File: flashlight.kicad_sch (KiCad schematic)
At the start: 42 parts, among them J1 USB_B_Micro, Q1 HSS2333, Q2 HSS2333, SW1 SW_DIP_x01, U1 LP4054HB5F, U2 MT3608

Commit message: v0.1
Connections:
- net GND: now also R3.1; no longer D3.1 (K)
- net at C1.1, D1.1 (K), D2.2 (A)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: now also U1.4 (V_{DD})
- net at R2.2, U1.1 (STAT): now also D3.2 (A); no longer R3.1
- net at R3.2: now also D3.1 (K); no longer D3.2 (A)
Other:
- moved on the sheet: D3, R3
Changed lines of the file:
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@@
   (junction (at 259.08 58.42) (diameter 0) (color 0 0 0 0)
   )
-  (junction (at 85.09 101.6) (diameter 0) (color 0 0 0 0)
-  )
   (junction (at 30.48 138.43) (diameter 0) (color 0 0 0 0)
   )
+  (junction (at 68.58 101.6) (diameter 0) (color 0 0 0 0)
+  )
   (junction (at 90.17 148.59) (diameter 0) (color 0 0 0 0)
   )
@@
   )
   (junction (at 144.78 58.42) (diameter 0) (color 0 0 0 0)
+  )
+  (junction (at 111.76 58.42) (diameter 0) (color 0 0 0 0)
   )
   (junction (at 241.3 58.42) (diameter 0) (color 0 0 0 0)
@@
     (stroke (width 0) (type default))
   )
+  (wire (pts (xy 68.58 101.6) (xy 68.58 102.87))
+    (stroke (width 0) (type default))
+  )
   (wire (pts (xy 241.3 58.42) (xy 241.3 72.39))
     (stroke (width 0) (type default))
@@
     (stroke (width 0) (type default))
   )
+  (wire (pts (xy 111.76 58.42) (xy 144.78 58.42))
+    (stroke (width 0) (type default))
+  )
   (wire (pts (xy 233.68 58.42) (xy 241.3 58.42))
     (stroke (width 0) (type default))
@@
     (stroke (width 0) (type default))
   )
+  (wire (pts (xy 68.58 113.03) (xy 82.55 113.03))
+    (stroke (width 0) (type default))
+  )
   (wire (pts (xy 90.17 158.75) (xy 90.17 163.83))
     (stroke (width 0) (type default))
@@
     (stroke (width 0) (type default))
   )
-  (wire (pts (xy 85.09 101.6) (xy 125.73 101.6))
+  (wire (pts (xy 68.58 101.6) (xy 125.73 101.6))
     (stroke (width 0) (type default))
   )
@@
     (stroke (width 0) (type default))
   )
-  (wire (pts (xy 85.09 73.66) (xy 85.09 83.82))
-    (stroke (width 0) (type default))
-  )
   (wire (pts (xy 53.34 58.42) (xy 68.58 58.42))
     (stroke (width 0) (type default))
   )
-  (wire (pts (xy 93.98 67.31) (xy 93.98 63.5))
-    (stroke (width 0) (type default))
-  )
   (wire (pts (xy 259.08 58.42) (xy 270.51 58.42))
     (stroke (width 0) (type default))
@@
     (stroke (width 0) (type default))
   )
-  (wire (pts (xy 68.58 101.6) (xy 85.09 101.6))
-    (stroke (width 0) (type default))
-  )
   (wire (pts (xy 83.82 138.43) (xy 90.17 138.43))
     (stroke (width 0) (type default))
@@
     (stroke (width 0) (type default))
   )
+  (wire (pts (xy 93.98 116.84) (xy 93.98 113.03))
+    (stroke (width 0) (type default))
+  )
   (wire (pts (xy 259.08 58.42) (xy 259.08 64.77))
     (stroke (width 0) (type default))
   )
-  (wire (pts (xy 68.58 58.42) (xy 144.78 58.42))
+  (wire (pts (xy 68.58 58.42) (xy 111.76 58.42))
     (stroke (width 0) (type default))
   )
@@
     (stroke (width 0) (type default))
   )
+  (wire (pts (xy 93.98 113.03) (xy 90.17 113.03))
+    (stroke (width 0) (type default))
+  )
   (wire (pts (xy 76.2 148.59) (xy 71.12 148.59))
     (stroke (width 0) (type default))
@@
     (stroke (width 0) (type default))
   )
+  (wire (pts (xy 68.58 110.49) (xy 68.58 113.03))
+    (stroke (width 0) (type default))
+  )
   (wire (pts (xy 30.48 148.59) (xy 30.48 138.43))
     (stroke (width 0) (type default))
   )
-  (wire (pts (xy 85.09 91.44) (xy 85.09 101.6))
-    (stroke (width 0) (type default))
-  )
   (wire (pts (xy 134.62 95.25) (xy 134.62 99.06))
     (stroke (width 0) (type default))
@@
     (stroke (width 0) (type default))
   )
+  (wire (pts (xy 111.76 58.42) (xy 111.76 72.39))
+    (stroke (width 0) (type default))
+  )
   (wire (pts (xy 30.48 138.43) (xy 33.02 138.43))
     (stroke (width 0) (type default))
@@
   )
   (wire (pts (xy 134.62 85.09) (xy 147.32 85.09))
-    (stroke (width 0) (type default))
-  )
-  (wire (pts (xy 93.98 63.5) (xy 85.09 63.5))
-    (stroke (width 0) (type default))
-  )
-  (wire (pts (xy 85.09 63.5) (xy 85.09 66.04))
     (stroke (width 0) (type default))
   )
@@
     )
   )
-  (symbol (lib_id "power:GND") (at 93.98 67.31 0) (unit 1)
-    (in_bom yes) (on_board yes) (dnp no) (fields_autoplaced)
-    (property "Reference" "#PWR05" (at 93.98 73.66 0)
-      (effects (font (size 1.27 1.27)) hide)
-    )
-    (property "Value" "GND" (at 96.52 68.58 0)
-      (effects (font (size 1.27 1.27)) (justify left))
-    )
-    (property "Footprint" "" (at 93.98 67.31 0)
-      (effects (font (size 1.27 1.27)) hide)
-    )
-    (property "Datasheet" "" (at 93.98 67.31 0)
+  (symbol (lib_id "power:GND") (at 93.98 116.84 0) (unit 1)
+    (in_bom yes) (on_board yes) (dnp no) (fields_autoplaced)
+    (property "Reference" "#PWR05" (at 93.98 123.19 0)
+      (effects (font (size 1.27 1.27)) hide)
+    )
+    (property "Value" "GND" (at 96.52 118.11 0)
+      (effects (font (size 1.27 1.27)) (justify left))
+    )
+    (property "Footprint" "" (at 93.98 116.84 0)
+      (effects (font (size 1.27 1.27)) hide)
+    )
+    (property "Datasheet" "" (at 93.98 116.84 0)
       (effects (font (size 1.27 1.27)) hide)
     )
@@
     )
   )
-  (symbol (lib_id "Device:LED") (at 85.09 69.85 270) (unit 1)
-    (in_bom yes) (on_board yes) (dnp no) (fields_autoplaced)
-    (property "Reference" "D3" (at 81.28 69.5325 90)
+  (symbol (lib_id "Device:LED") (at 68.58 106.68 90) (unit 1)
+    (in_bom yes) (on_board yes) (dnp no) (fields_autoplaced)
+    (property "Reference" "D3" (at 72.39 106.9975 90)
       (effects (font (size 1.27 1.27)) (justify right))
     )
-    (property "Value" "GREEN" (at 81.28 66.9925 90)
+    (property "Value" "GREEN" (at 72.39 109.5375 90)
       (effects (font (size 1.27 1.27)) (justify right))
     )
-    (property "Footprint" "LED_SMD:LED_0603_1608Metric" (at 85.09 69.85 0)
-      (effects (font (size 1.27 1.27)) hide)
-    )
-    (property "Datasheet" "~" (at 85.09 69.85 0)
-      (effects (font (size 1.27 1.27)) hide)
-    )
-    (property "LCSC" "C205451" (at 85.09 69.85 90)
+    (property "Footprint" "LED_SMD:LED_0603_1608Metric" (at 68.58 106.68 0)
+      (effects (font (size 1.27 1.27)) hide)
+    )
+    (property "Datasheet" "~" (at 68.58 106.68 0)
+      (effects (font (size 1.27 1.27)) hide)
+    )
+    (property "LCSC" "C205451" (at 68.58 106.68 90)
       (effects (font (size 1.27 1.27)) hide)
     )
@@
     )
   )
-  (symbol (lib_id "Device:R") (at 85.09 87.63 180) (unit 1)
-    (in_bom yes) (on_board yes) (dnp no) (fields_autoplaced)
-    (property "Reference" "R3" (at 82.55 88.9 0)
-      (effects (font (size 1.27 1.27)) (justify left))
-    )
-    (property "Value" "499" (at 82.55 86.36 0)
-      (effects (font (size 1.27 1.27)) (justify left))
-    )
-    (property "Footprint" "Resistor_SMD:R_0805_2012Metric_Pad1.20x1.40mm_HandSolder" (at 86.868 87.63 90)
-      (effects (font (size 1.27 1.27)) hide)
-    )
-    (property "Datasheet" "~" (at 85.09 87.63 0)
-      (effects (font (size 1.27 1.27)) hide)
-    )
-    (property "LCSC" "C5200556" (at 85.09 87.63 0)
-      (effects (font (size 1.27 1.27)) hide)
-    )
+  (symbol (lib_id "Device:R") (at 86.36 113.03 270) (unit 1)
+    (in_bom yes) (on_board yes) (dnp no) (fields_autoplaced)
+    (property "Reference" "R3" (at 86.36 106.68 90)
+      (effects (font (size 1.27 1.27)))
+    )
+    (property "Value" "499" (at 86.36 109.22 90)
+      (effects (font (size 1.27 1.27)))
+    )
+    (property "Footprint" "Resistor_SMD:R_0805_2012Metric_Pad1.20x1.40mm_HandSolder" (at 86.36 111.252 90)
+      (effects (font (size 1.27 1.27)) hide)
+    )
+    (property "Datasheet" "~" (at 86.36 113.03 0)
+      (effects (font (size 1.27 1.27)) hide)
+    )
+    (property "LCSC" "C5200556" (at 86.36 113.03 0)
+      (effects (font (size 1.27 1.27)) hide)
+    )

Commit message: jlcpcb completed
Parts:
- J1: LCSC (none) -> C2858269; LSCS C2858269 -> (none)
- R7: LCSC (none) -> C2999631
- U1: LCSC (none) -> C517187
- U2: LCSC (none) -> C84817
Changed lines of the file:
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@@
+      (effects (font (size 1.27 1.27)) hide)
+    )
+    (property "LCSC" "C517187" (at 111.76 80.01 0)
       (effects (font (size 1.27 1.27)) hide)
     )
@@
       (effects (font (size 1.27 1.27)) hide)
     )
-    (property "LCSC" "" (at 259.08 68.58 0)
+    (property "LCSC" "C2999631" (at 259.08 68.58 0)
       (effects (font (size 1.27 1.27)) hide)
     )
@@
       (effects (font (size 1.27 1.27)) hide)
     )
-    (property "LSCS" "C2858269" (at 27.94 63.5 0)
+    (property "LCSC" "C2858269" (at 27.94 63.5 0)
       (effects (font (size 1.27 1.27)) hide)
     )
@@
       (effects (font (size 1.27 1.27)) hide)
     )
+    (property "LCSC" "C84817" (at 229.87 74.93 0)
+      (effects (font (size 1.27 1.27)) hide)
+    )

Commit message: led strip
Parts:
- removed D10, D11, D12, D13, D14, D15, D16, D17, D18, D19, D20, D6, D7, D8, D9: ~, FlashlightLib:SMD3014, symbol Device:LED
- removed R10, R8, R9: 169, Resistor_SMD:R_0805_2012Metric_Pad1.20x1.40mm_HandSolder, symbol Device:R
- added J2: Conn_01x03_Pin, FlashlightLib:LED_Strip, symbol Connector:Conn_01x03_Pin
- C1: value 4u7/10V -> 22uF/25V; footprint Capacitor_SMD:C_0603_1608Metric -> Capacitor_SMD:C_0805_2012Metric; LCSC C961503 -> C513764
- C2: value 4u7/10V -> 22uF/25V; footprint Capacitor_SMD:C_0603_1608Metric -> Capacitor_SMD:C_0805_2012Metric; LCSC (none) -> C513764
- C3, C4: footprint Capacitor_SMD:C_0603_1608Metric -> Capacitor_SMD:C_0805_2012Metric; LCSC C513775 -> C513764
- D1, D4, D5: footprint Diode_SMD:D_SOD-323 -> Diode_SMD:D_SMB; LCSC C727114 -> C4749013
- L1: footprint Inductor_SMD:L_0603_1608Metric -> FlashlightLib:L_5.0x5.0; LCSC C2941569 -> C2849501
- R1: value 2k2 -> 1k; footprint Resistor_SMD:R_0603_1608Metric -> Resistor_SMD:R_0805_2012Metric_Pad1.20x1.40mm_HandSolder; LCSC C3152135 -> C17513
- R2, R3: value 499 -> 1k; LCSC C5200556 -> C17513
- R4: value 2k2 -> 10k; footprint Resistor_SMD:R_0603_1608Metric -> Resistor_SMD:R_0805_2012Metric; LCSC C3152135 -> C3152175
- R6: footprint Resistor_SMD:R_0805_2012Metric_Pad1.20x1.40mm_HandSolder -> Resistor_SMD:R_0805_2012Metric
- R7: value 294k -> 191k; LCSC C2999631 -> C865240; now left out of the parts list
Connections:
- net GND: now also R3.2, J2.2 (Pin_2), J2.3 (Pin_3); no longer R3.1
- net VDD: now also J2.1 (Pin_1)
- net at D3.1 (K): now also R3.1; no longer R3.2
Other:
- note added: "2k2"
- note added: "4u7/10V"

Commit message: JLCPCB ordered
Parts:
- added D12, D6, D9: ~, FlashlightLib:SMD3014, symbol Device:LED
- added R5: 169, Resistor_SMD:R_0805_2012Metric_Pad1.20x1.40mm_HandSolder, symbol Device:R
- D1, D4, D5: LCSC C4749013 -> C5338051
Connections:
- net GND: now also R5.2
- net VDD: now also D6.2 (A)
- new net: D12.1 (K), R5.1
- new net: D12.2 (A), D9.1 (K)
- new net: D6.1 (K), D9.2 (A)
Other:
- moved on the sheet: J2

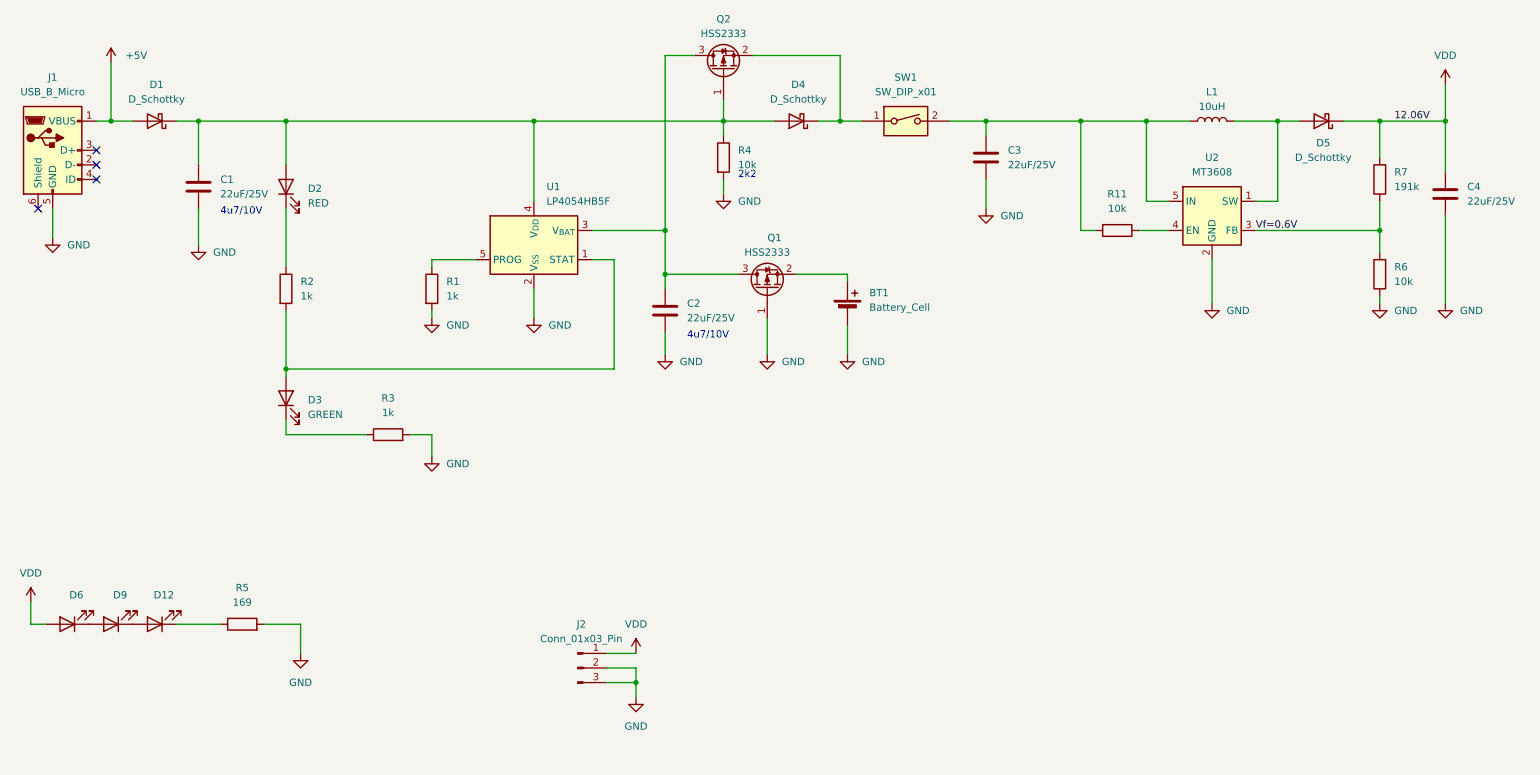
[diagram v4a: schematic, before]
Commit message: shortened GND paths
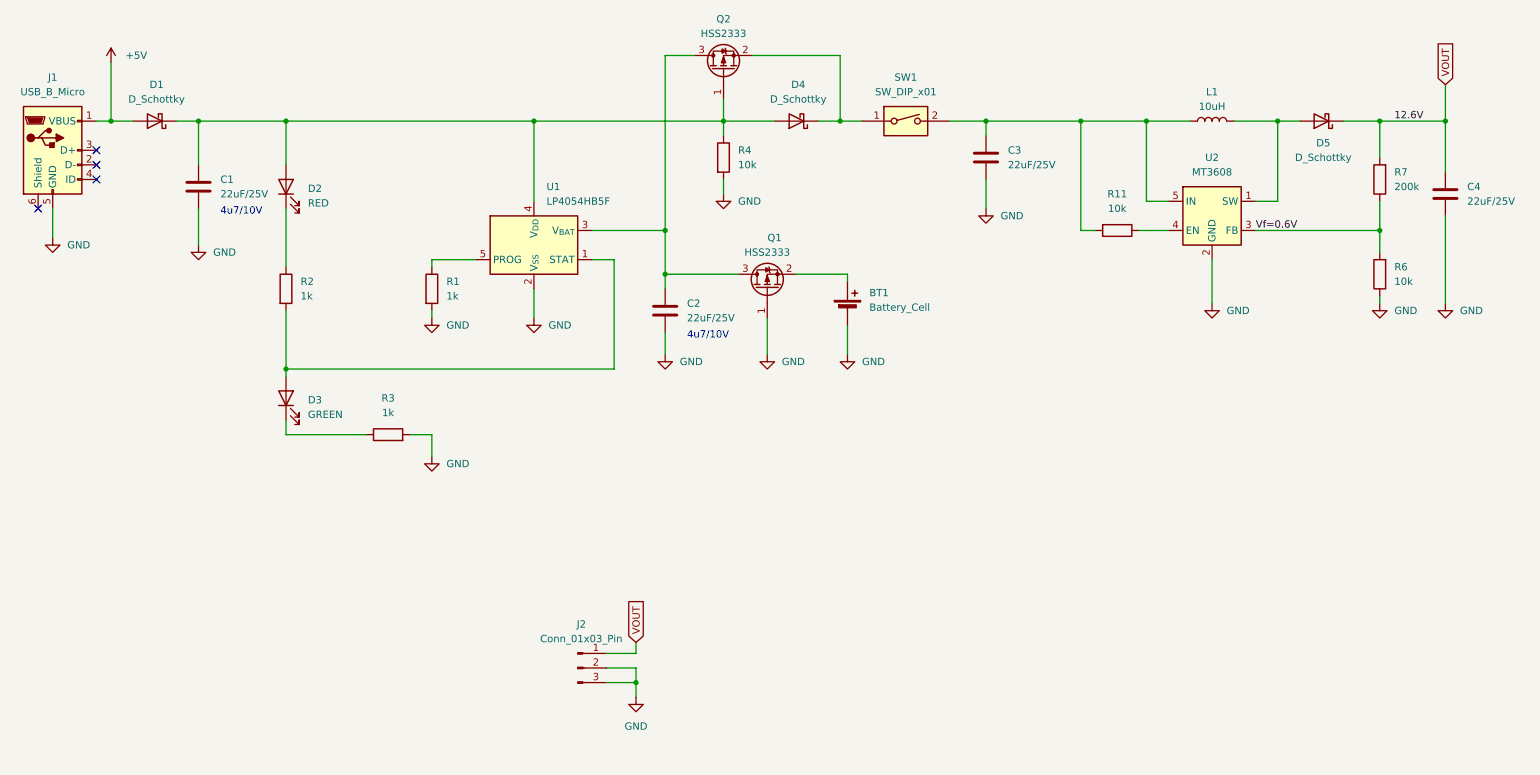
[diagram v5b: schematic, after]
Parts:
- removed D12, D6, D9: ~, FlashlightLib:SMD3014, symbol Device:LED
- removed R5: 169, Resistor_SMD:R_0805_2012Metric_Pad1.20x1.40mm_HandSolder, symbol Device:R
- C1, C2, C4: LCSC C513764 -> C45783
- D1, D4: LCSC C5338051 -> C22452
- D2: LCSC C497932 -> C2286
- D3: footprint LED_SMD:LED_0603_1608Metric -> LED_SMD:LED_0805_2012Metric; LCSC C205451 -> C2297
- R1, R2, R3: footprint Resistor_SMD:R_0805_2012Metric_Pad1.20x1.40mm_HandSolder -> Resistor_SMD:R_0805_2012Metric
- R11, R4, R6: LCSC C3152175 -> C17414
- R7: value 191k -> 200k; LCSC C865240 -> C17539
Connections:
- net VDD renamed VOUT
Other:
- note removed: "2k2"

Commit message: upd v2.2
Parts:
- R7: footprint Resistor_SMD:R_0805_2012Metric_Pad1.20x1.40mm_HandSolder -> Resistor_SMD:R_0805_2012Metric
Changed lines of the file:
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@@
       (effects (font (size 1.27 1.27)) (justify right))
     )
-    (property "Footprint" "Resistor_SMD:R_0805_2012Metric_Pad1.20x1.40mm_HandSolder" (at 260.858 68.58 90)
+    (property "Footprint" "Resistor_SMD:R_0805_2012Metric" (at 260.858 68.58 90)
       (effects (font (size 1.27 1.27)) hide)
     )

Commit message: 0603 footprint
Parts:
- R11, R4, R6: footprint Resistor_SMD:R_0805_2012Metric -> Resistor_SMD:R_0603_1608Metric; LCSC C17414 -> C25804
- R7: footprint Resistor_SMD:R_0805_2012Metric -> Resistor_SMD:R_0603_1608Metric; LCSC C17539 -> C25811; now in the parts list
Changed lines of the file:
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@@
       (effects (font (size 1.27 1.27)))
     )
-    (property "Footprint" "Resistor_SMD:R_0805_2012Metric" (at 213.36 75.692 90)
+    (property "Footprint" "Resistor_SMD:R_0603_1608Metric" (at 213.36 75.692 90)
       (effects (font (size 1.27 1.27)) hide)
     )
@@
       (effects (font (size 1.27 1.27)) hide)
     )
-    (property "LCSC" "C17414" (at 213.36 77.47 0)
+    (property "LCSC" "C25804" (at 213.36 77.47 0)
       (effects (font (size 1.27 1.27)) hide)
     )
@@
       (effects (font (size 1.27 1.27)) (justify left))
     )
-    (property "Footprint" "Resistor_SMD:R_0805_2012Metric" (at 143.002 64.77 90)
+    (property "Footprint" "Resistor_SMD:R_0603_1608Metric" (at 143.002 64.77 90)
       (effects (font (size 1.27 1.27)) hide)
     )
@@
       (effects (font (size 1.27 1.27)) hide)
     )
-    (property "LCSC" "C17414" (at 144.78 64.77 0)
+    (property "LCSC" "C25804" (at 144.78 64.77 0)
       (effects (font (size 1.27 1.27)) hide)
     )
@@
   )
   (symbol (lib_id "Device:R") (at 259.08 68.58 180) (unit 1)
-    (in_bom no) (on_board yes) (dnp no) (fields_autoplaced)
+    (in_bom yes) (on_board yes) (dnp no) (fields_autoplaced)
     (property "Reference" "R7" (at 261.62 67.31 0)
       (effects (font (size 1.27 1.27)) (justify right))
@@
       (effects (font (size 1.27 1.27)) (justify right))
     )
-    (property "Footprint" "Resistor_SMD:R_0805_2012Metric" (at 260.858 68.58 90)
+    (property "Footprint" "Resistor_SMD:R_0603_1608Metric" (at 260.858 68.58 90)
       (effects (font (size 1.27 1.27)) hide)
     )
@@
       (effects (font (size 1.27 1.27)) hide)
     )
-    (property "LCSC" "C17539" (at 259.08 68.58 0)
+    (property "LCSC" "C25811" (at 259.08 68.58 0)
       (effects (font (size 1.27 1.27)) hide)
     )
@@
       (effects (font (size 1.27 1.27)) (justify right))
     )
-    (property "Footprint" "Resistor_SMD:R_0805_2012Metric" (at 260.858 85.09 90)
+    (property "Footprint" "Resistor_SMD:R_0603_1608Metric" (at 260.858 85.09 90)
       (effects (font (size 1.27 1.27)) hide)
     )
@@
       (effects (font (size 1.27 1.27)) hide)
     )
-    (property "LCSC" "C17414" (at 259.08 85.09 0)
-      (effects (font (size 1.27 1.27)) hide)
-    )
+    (property "LCSC" "C25804" (at 259.08 85.09 0)
+      (effects (font (size 1.27 1.27)) hide)
+    )
